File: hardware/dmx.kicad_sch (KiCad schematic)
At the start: 38 parts, among them J101 Cortex_Debug, J102 DX07S016JA3, SW101 SKSG, SW102 SKSG, U101 TPS78433QWDRBRQ1, U102 ATSAMD51G, Y101 32k768

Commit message: Refresh
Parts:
- C101: Rating (none) -> 10V
- C102, C103, C104, C105: Rating (none) -> 50V
- D103: Mouser 755-SML-D12M8WT86C -> 755-SML-D12D1WT86; Product SML-D12M8WT86C -> SML-D12D1WT86
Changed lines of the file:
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@@
 			)
 		)
+		(property "Rating" "50V"
+			(at 115.57 46.99 0)
+			(effects
+				(font
+					(size 1.27 1.27)
+				)
+				(hide yes)
+			)
+		)
 		(pin "1"
 		)
@@
 			)
 		)
-		(property "Description" "Power symbol creates a global label with name \"GND\" , ground"
+		(property "Description" ""
 			(at 270.256 71.374 0)
 			(effects
@@
 			)
 		)
-		(property "Description" "Power symbol creates a global label with name \"+3V3\""
+		(property "Description" ""
 			(at 205.74 54.356 0)
 			(effects
@@
 			)
 		)
-		(property "Description" "Power symbol creates a global label with name \"Earth\""
+		(property "Description" ""
 			(at 266.192 78.74 0)
 			(effects
@@
 			)
 		)
-		(property "Description" "Power symbol creates a global label with name \"GND\" , ground"
+		(property "Description" ""
 			(at 103.124 43.434 0)
 			(effects
@@
 			)
 		)
-		(property "Description" "Power symbol creates a global label with name \"GND\" , ground"
+		(property "Description" ""
 			(at 228.854 99.314 0)
 			(effects
@@
 			)
 		)
-		(property "Description" "Power symbol creates a global label with name \"GND\" , ground"
+		(property "Description" ""
 			(at 73.406 137.414 0)
 			(effects
@@
 			)
 		)
-		(property "Description" "Power symbol creates a global label with name \"GND\" , ground"
+		(property "Description" ""
 			(at 36.576 59.944 0)
 			(effects
@@
 			)
 		)
-		(property "Description" "Power symbol creates a global label with name \"+5V\""
+		(property "Description" ""
 			(at 247.142 105.41 0)
 			(effects
@@
 			)
 		)
-		(property "Mouser" "755-SML-D12M8WT86C"
+		(property "Mouser" "755-SML-D12D1WT86"
 			(at 130.556 45.72 0)
 			(effects
@@
 			)
 		)
-		(property "Product" "SML-D12M8WT86C "
+		(property "Product" "SML-D12D1WT86"
 			(at 129.54 45.72 0)
 			(effects
@@
 			)
 		)
-		(property "Description" "Power symbol creates a global label with name \"GND\" , ground"
+		(property "Description" ""
 			(at 63.246 37.084 0)
 			(effects
@@
 			)
 		)
-		(property "Description" "Power symbol creates a global label with name \"Earth\""
+		(property "Description" ""
 			(at 181.61 137.922 0)
 			(effects
@@
 			)
 		)
-		(property "Description" "Power symbol creates a global label with name \"+3V3\""
+		(property "Description" ""
 			(at 78.74 36.576 0)
 			(effects
@@
 			)
 		)
-		(property "Description" "Power symbol creates a global label with name \"+5V\""
+		(property "Description" ""
 			(at 270.51 62.738 0)
 			(effects
@@
 			)
 		)
-		(property "Description" "Power symbol creates a global label with name \"+3V3\""
+		(property "Description" ""
 			(at 69.596 121.92 0)
 			(effects
@@
 			)
 		)
-		(property "Sim.Enable" "0"
-			(at 128.27 97.79 0)
-			(effects
-				(font
-					(size 1.27 1.27)
-				)
-				(hide yes)
-			)
-		)
 		(pin "1"
 		)
@@
 			)
 		)
-		(property "Description" "Power symbol creates a global label with name \"GND\" , ground"
+		(property "Description" ""
 			(at 31.496 59.944 0)
 			(effects
@@
 			)
 		)
-		(property "Description" "Power symbol creates a global label with name \"GND\" , ground"
+		(property "Description" ""
 			(at 106.426 102.616 0)
 			(effects
@@
 			)
 		)
-		(property "Description" "Power symbol creates a global label with name \"GND\" , ground"
+		(property "Description" ""
 			(at 188.976 137.414 0)
 			(effects
@@
 			)
 		)
-		(property "Description" "Power symbol creates a global label with name \"+5V\""
+		(property "Description" ""
 			(at 180.34 53.848 0)
 			(effects
@@
 			)
 		)
-		(property "Description" "Power symbol creates a global label with name \"GND\" , ground"
+		(property "Description" ""
 			(at 228.854 96.774 0)
 			(effects
@@
 			)
 		)
-		(property "Description" "Power symbol creates a global label with name \"+3V3\""
+		(property "Description" ""
 			(at 74.676 48.26 0)
 			(effects
@@
 			)
 		)
-		(property "Description" "Power symbol creates a global label with name \"GND\" , ground"
+		(property "Description" ""
 			(at 84.836 37.084 0)
 			(effects
@@
 			)
 		)
-		(property "Description" "Power symbol creates a global label with name \"GND\" , ground"
+		(property "Description" ""
 			(at 238.506 28.956 0)
 			(effects
@@
 			)
 		)
-		(property "Description" "Power symbol creates a global label with name \"+3V3\""
+		(property "Description" ""
 			(at 131.826 92.71 0)
 			(effects
@@
 			)
 		)
+		(property "Rating" "10V"
+			(at 63.5 49.53 0)
+			(effects
+				(font
+					(size 1.27 1.27)
+				)
+				(hide yes)
+			)
+		)
 		(pin "1"
 		)
@@
 			)
 		)
-		(property "Description" "Power symbol creates a global label with name \"+5V\""
+		(property "Description" ""
 			(at 201.93 100.838 0)
 			(effects
@@
 			)
 		)
-		(property "Description" "Power symbol creates a global label with name \"GND\" , ground"
+		(property "Description" ""
 			(at 180.086 54.864 0)
 			(effects
@@
 			)
 		)
-		(property "Description" "Power symbol creates a global label with name \"GND\" , ground"
+		(property "Description" ""
 			(at 192.786 59.944 0)
 			(effects
@@
 			)
 		)
-		(property "Description" "Power symbol creates a global label with name \"+5V\""
+		(property "Description" ""
 			(at 240.792 82.55 0)
 			(effects
@@
 			)
 		)
-		(property "Description" "Power symbol creates a global label with name \"GND\" , ground"
+		(property "Description" ""
 			(at 151.384 58.674 0)
 			(effects
@@
 			)
 		)
-		(property "Description" "Power symbol creates a global label with name \"GND\" , ground"
+		(property "Description" ""
 			(at 272.034 108.204 0)
 			(effects
@@
 			)
 		)
+		(property "Rating" "50V"
+			(at 105.41 46.99 0)
+			(effects
+				(font
+					(size 1.27 1.27)
+				)
+				(hide yes)
+			)
+		)
 		(pin "1"
 		)
@@
 			)
 		)
-		(property "Description" "Power symbol creates a global label with name \"GND\" , ground"
+		(property "Description" ""
 			(at 205.486 54.864 0)
 			(effects
@@
 			)
 		)
+		(property "Rating" "50V"
+			(at 85.09 46.99 0)
+			(effects
+				(font
+					(size 1.27 1.27)
+				)
+				(hide yes)
+			)
+		)
 		(pin "1"
 		)
@@
 			)
 		)
-		(property "Description" "Power symbol creates a global label with name \"GND\" , ground"
+		(property "Description" ""
 			(at 265.684 86.614 0)
 			(effects
@@
 			)
 		)
-		(property "Description" "Power symbol creates a global label with name \"GND\" , ground"
+		(property "Description" ""
 			(at 114.046 75.946 0)
 			(effects
@@
 			(effects
 				(font
+					(size 1.27 1.27)
+				)
+				(hide yes)
+			)
+		)
+		(property "Rating" "50V"
+			(at 95.25 46.99 0)
+			(effects
+				(font

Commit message: Update library
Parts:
- J101: value Cortex_Debug -> Cortex; footprint V2_Cortex_Debug:Cortex_Debug_Pad -> V2_Connector_Debug:Cortex; symbol V2_Cortex_Debug:Cortex_Debug -> V2_Connector_Debug:Cortex
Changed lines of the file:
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@@
 	)
 	(symbol
-		(lib_id "V2_Cortex_Debug:Cortex_Debug")
+		(lib_id "V2_Connector_Debug:Cortex")
 		(at 128.27 97.79 0)
 		(unit 1)
@@
 			)
 		)
-		(property "Value" "Cortex_Debug"
+		(property "Value" "Cortex"
 			(at 129.54 87.63 0)
 			(effects
@@
 			)
 		)
-		(property "Footprint" "V2_Cortex_Debug:Cortex_Debug_Pad"
+		(property "Footprint" "V2_Connector_Debug:Cortex"
 			(at 128.27 111.76 0)
 			(effects

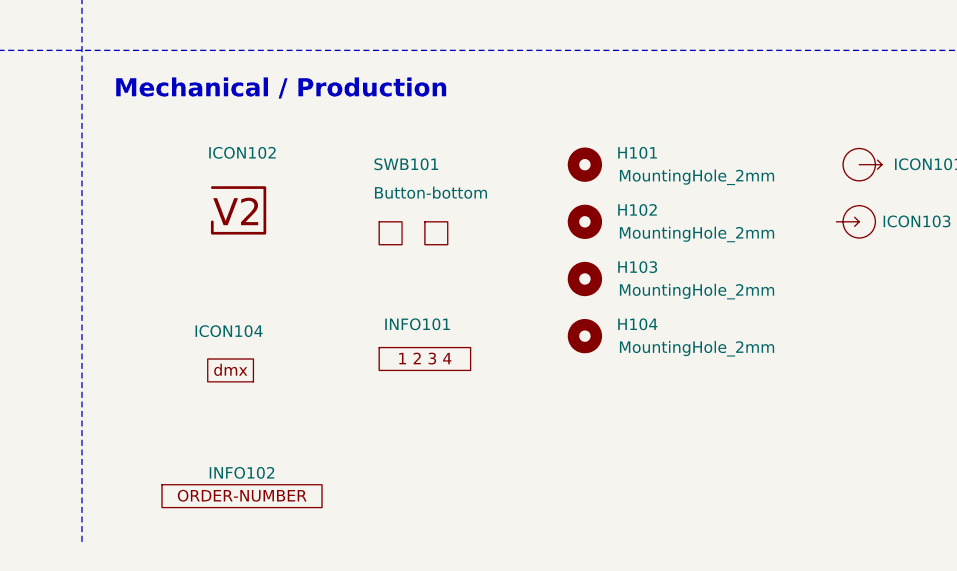
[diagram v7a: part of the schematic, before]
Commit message: Replace Order_Number
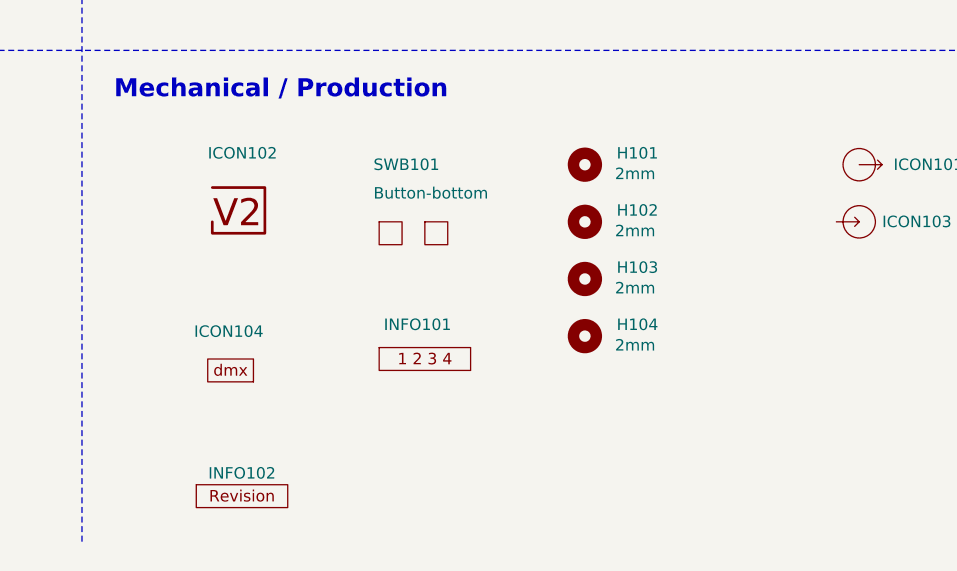
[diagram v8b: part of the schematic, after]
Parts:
- H101, H102, H103, H104: value MountingHole_2mm -> 2mm
- INFO102: value Order_Number -> (none); footprint V2_Production:Order_Number -> V2_Production:Revision; symbol V2_Production:Order_Number -> V2_Production:Revision
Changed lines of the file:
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@@
 		(at 250.19 154.94 0)
 		(unit 1)
-		(exclude_from_sim yes)
+		(exclude_from_sim no)
 		(in_bom no)
 		(on_board yes)
@@
 			)
 		)
+		(property "Sim.Enable" "0"
+			(at 250.19 154.94 0)
+			(effects
+				(font
+					(size 1.27 1.27)
+				)
+				(hide yes)
+			)
+		)
 		(instances
 			(project "dmx"
@@
 		(at 219.71 154.94 0)
 		(unit 1)
-		(exclude_from_sim yes)
+		(exclude_from_sim no)
 		(in_bom no)
 		(on_board yes)
@@
 			)
 		)
-		(property "Value" "MountingHole_2mm"
-			(at 232.156 156.21 0)
+		(property "Value" "2mm"
+			(at 225.298 155.956 0)
 			(effects
 				(font
@@
 		(at 219.71 161.29 0)
 		(unit 1)
-		(exclude_from_sim yes)
+		(exclude_from_sim no)
 		(in_bom no)
 		(on_board yes)
@@
 			)
 		)
-		(property "Value" "MountingHole_2mm"
-			(at 232.156 162.56 0)
+		(property "Value" "2mm"
+			(at 225.298 162.306 0)
 			(effects
 				(font
@@
 		(at 200.66 162.56 0)
 		(unit 1)
-		(exclude_from_sim yes)
+		(exclude_from_sim no)
 		(in_bom no)
 		(on_board yes)
@@
 			)
 		)
+		(property "Sim.Enable" "0"
+			(at 200.66 162.56 0)
+			(effects
+				(font
+					(size 1.27 1.27)
+				)
+				(hide yes)
+			)
+		)
 		(instances
 			(project "dmx"
@@
 		(at 219.71 167.64 0)
 		(unit 1)
-		(exclude_from_sim yes)
+		(exclude_from_sim no)
 		(in_bom no)
 		(on_board yes)
@@
 			)
 		)
-		(property "Value" "MountingHole_2mm"
-			(at 232.156 168.91 0)
+		(property "Value" "2mm"
+			(at 225.298 168.656 0)
 			(effects
 				(font
@@
 	)
 	(symbol
-		(lib_id "V2_Production:Order_Number")
+		(lib_id "V2_Production:Revision")
 		(at 181.61 191.77 0)
 		(unit 1)
@@
 			)
 		)
-		(property "Value" "Order_Number"
+		(property "Value" ""
 			(at 181.61 194.31 0)
 			(effects
@@
 			)
 		)
-		(property "Footprint" "V2_Production:Order_Number"
+		(property "Footprint" "V2_Production:Revision"
 			(at 181.61 196.85 0)
 			(effects
@@
 		(at 219.71 173.99 0)
 		(unit 1)
-		(exclude_from_sim yes)
+		(exclude_from_sim no)
 		(in_bom no)
 		(on_board yes)
@@
 			)
 		)
-		(property "Value" "MountingHole_2mm"
-			(at 232.156 175.26 0)
+		(property "Value" "2mm"
+			(at 225.298 175.006 0)
 			(effects
 				(font
@@
 		(at 180.34 177.8 0)
 		(unit 1)
-		(exclude_from_sim yes)
+		(exclude_from_sim no)
 		(in_bom no)
 		(on_board yes)
@@
 			)
 		)
+		(property "Sim.Enable" "0"
+			(at 180.34 177.8 0)
+			(effects
+				(font
+					(size 1.27 1.27)
+				)
+				(hide yes)
+			)
+		)
 		(instances
 			(project "dmx"
@@
 		(at 250.19 161.29 0)
 		(unit 1)
-		(exclude_from_sim yes)
+		(exclude_from_sim no)
 		(in_bom no)
 		(on_board yes)
@@
 			)
 		)
+		(property "Sim.Enable" "0"
+			(at 250.19 161.29 0)
+			(effects
+				(font
+					(size 1.27 1.27)
+				)
+				(hide yes)
+			)
+		)
 		(instances
 			(project "dmx"
@@
 		(at 181.61 160.02 0)
 		(unit 1)
-		(exclude_from_sim yes)
+		(exclude_from_sim no)
 		(in_bom no)
 		(on_board yes)
